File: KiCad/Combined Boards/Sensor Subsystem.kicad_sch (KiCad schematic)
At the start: 5 parts, among them J1 Conn_01x12, U1 74HC165, U3 74LVC1G125DBVR, U4 DS18B20U

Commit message: Started Central Subsystem
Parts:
- renumbered U3 to U2, U4 to U3
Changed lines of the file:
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@@
   (symbol (lib_id "Sensor_Temperature:DS18B20U") (at 71.12 100.33 0) (unit 1)
     (in_bom yes) (on_board yes) (dnp no) (fields_autoplaced)
-    (property "Reference" "U4" (at 64.77 99.695 0)
+    (property "Reference" "U3" (at 64.77 99.695 0)
       (effects (font (size 1.27 1.27)) (justify right))
     )
@@
       (project "Combined Boards"
         (path "/819f9f2e-5083-42df-b63a-6cdcb84600f5/0c64a068-0944-4527-8a78-19113e5af5d7"
-          (reference "U4") (unit 1)
+          (reference "U3") (unit 1)
         )
       )
@@
   (symbol (lib_id "74xGxx:74LVC1G125") (at 207.01 99.06 0) (unit 1)
     (in_bom yes) (on_board yes) (dnp no)
-    (property "Reference" "U3" (at 210.82 95.25 0)
+    (property "Reference" "U2" (at 210.82 95.25 0)
       (effects (font (size 1.27 1.27)))
     )
@@
       (project "Combined Boards"
         (path "/819f9f2e-5083-42df-b63a-6cdcb84600f5/0c64a068-0944-4527-8a78-19113e5af5d7"
-          (reference "U3") (unit 1)
+          (reference "U2") (unit 1)
         )
       )

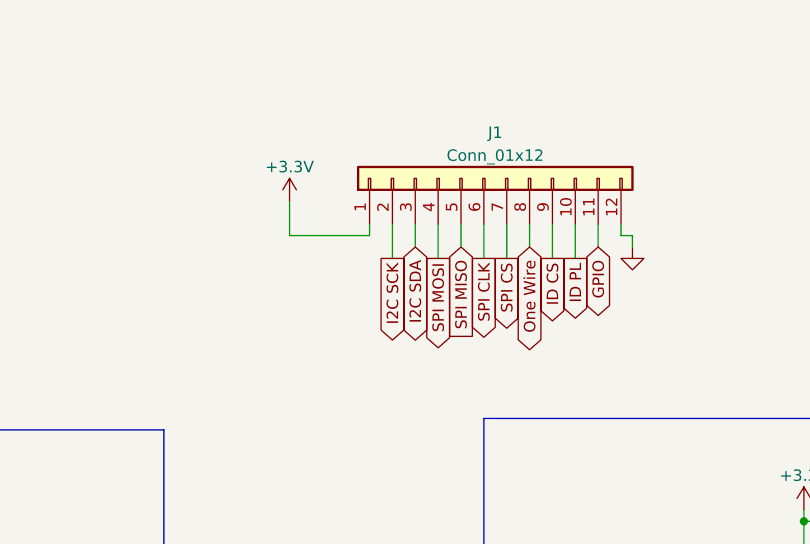
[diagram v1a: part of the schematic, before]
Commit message: Central subsystem design
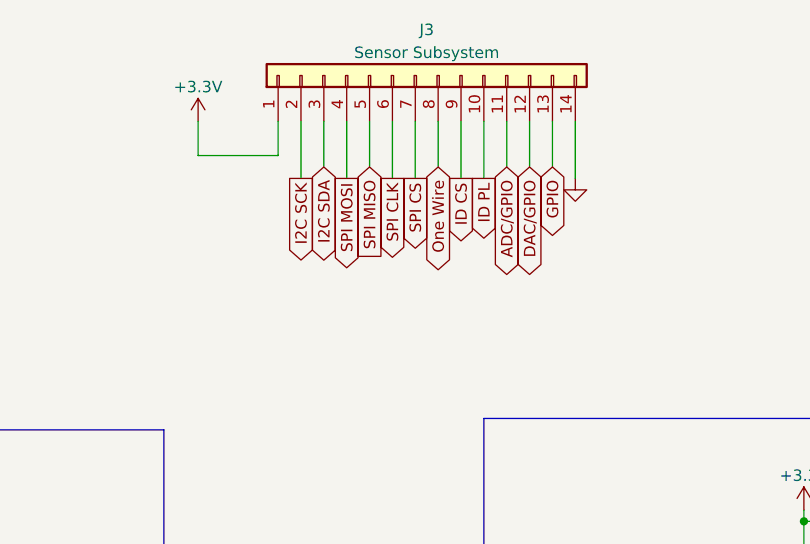
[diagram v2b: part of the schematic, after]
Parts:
- removed J1: Conn_01x12, symbol Connector_Generic:Conn_01x12
- added J3: Sensor Subsystem, symbol Connector_Generic:Conn_01x14
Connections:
- net +3.3V: now also J3.1 (Pin_1)
- net GND: now also J3.14 (Pin_14)
- net GPIO: now also J3.13 (Pin_13)
- net I2C SCK: now also J3.2 (Pin_2)
- net I2C SDA: now also J3.3 (Pin_3)
- net ID CS: now also J3.9 (Pin_9)
- net ID PL: now also J3.10 (Pin_10)
- net One Wire: now also J3.8 (Pin_8)
- net SPI CLK: now also J3.6 (Pin_6)
- net SPI CS: now also J3.7 (Pin_7)
- net SPI MISO: now also J3.5 (Pin_5)
- net SPI MOSI: now also J3.4 (Pin_4)
- new net ADC/GPIO: J3.11 (Pin_11)
- new net DAC/GPIO: J3.12 (Pin_12)
